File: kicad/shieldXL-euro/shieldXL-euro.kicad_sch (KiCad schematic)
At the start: 0 parts

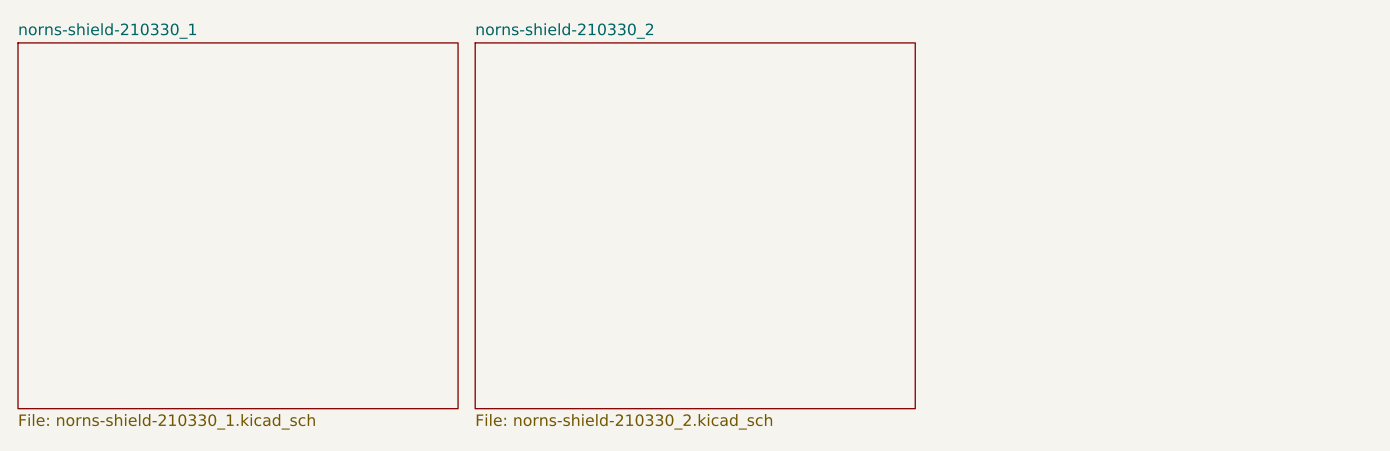
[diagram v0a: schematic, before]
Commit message: Add the Eurorack I/O sheet and the MMM footprint library
tools/make_eurorack_sheet.py writes eurorack.kicad_sch and hooks it into the
root as page 3: 10-pin rack power (op-amps only), 3.5 mm audio in/out through
a TL074 scaling 10 Vpp to the codec and back, PJ366ST MIDI jacks with Type A/B
on solder jumpers, USB-C power for the Pi through a polyfuse and TVS, and three
panel USB-A sockets cabled to the Pi. It joins the shield sheets by the global
labels the strip step placed.

strip_shield_io.py also removes the ground symbols left pinned to nothing once
the jacks were gone, in the same run as the strip. MMM.pretty and its 3D models
come from the Missing Mile Modular library; README.md covers the conversion,
the levels and what is left. Stop tracking __pycache__.

Co-Authored-By: Claude Opus 5.5 <noreply@anthropic.com>
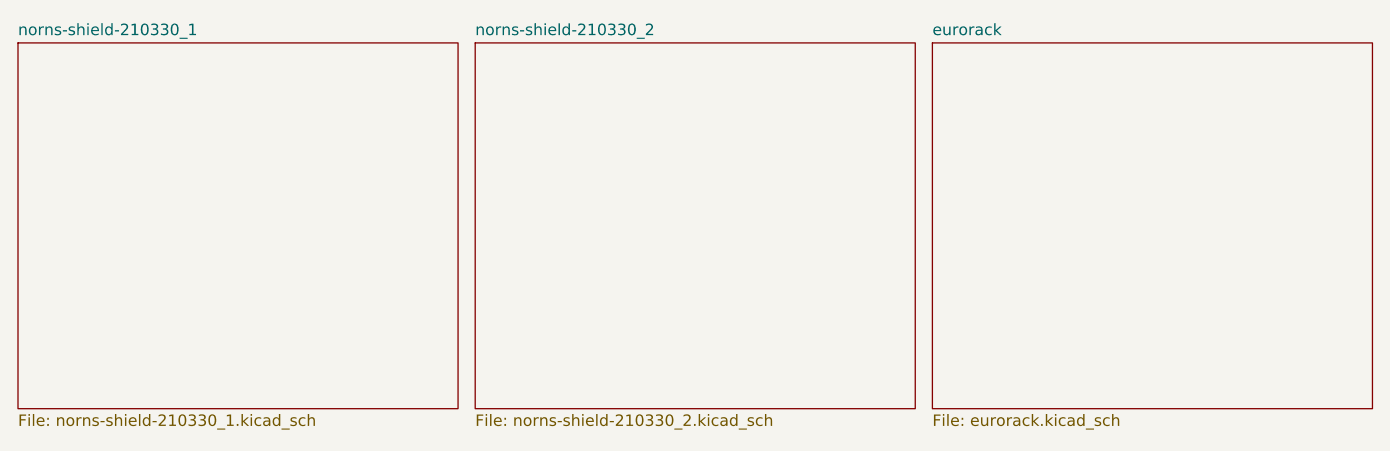
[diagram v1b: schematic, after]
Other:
- added sheet eurorack (eurorack.kicad_sch)
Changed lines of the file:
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@@
+		)
+	)
+	(sheet
+		(at 127 25.4)
+		(size 48.895 40.64)
+		(fields_autoplaced yes)
+		(stroke
+			(width 0)
+			(type solid)
+		)
+		(fill
+			(color 0 0 0 0.0000)
+		)
+		(property "Sheetname" "eurorack"
+			(at 127 24.6884 0)
+			(effects
+				(font
+					(size 1.27 1.27)
+				)
+				(justify left bottom)
+			)
+		)
+		(property "Sheetfile" "eurorack.kicad_sch"
+			(at 127 66.6246 0)
+			(effects
+				(font
+					(size 1.27 1.27)
+				)
+				(justify left top)
+			)
+		)
+		(instances
+			(project "shieldXL-euro"
+				(path "/b86e8947-58dc-49c6-bb5d-ce6d33c2e465"
+					(page "3")
+				)
+			)
 		)
 	)
